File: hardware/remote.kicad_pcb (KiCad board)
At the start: 2 copper layers, 40 x 25 mm, 26 parts, among them P1 CON-SENSOR2, P2 CONN_01X02, U1 XMC1XXX24, U2 RFM69HW, U3 DRILL, U4 DRILL, U5 DRILL, U6 DRILL

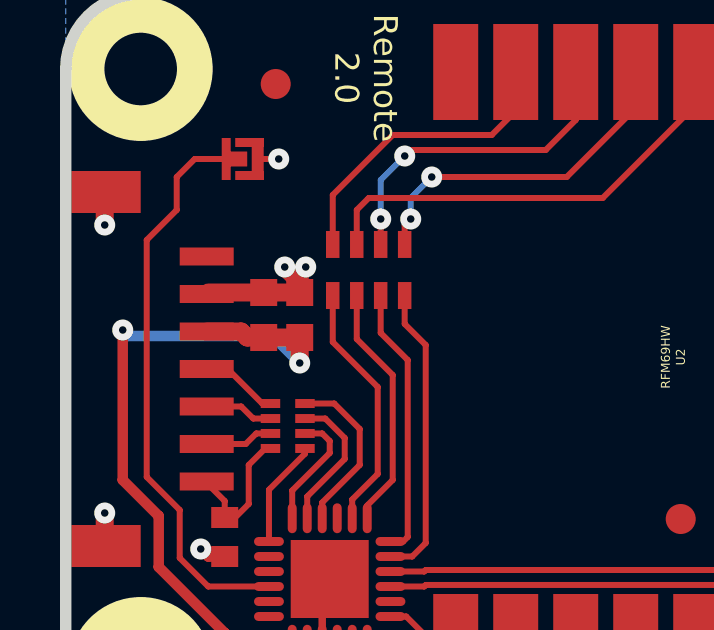
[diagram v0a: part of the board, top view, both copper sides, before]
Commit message: fix capacitor footprints
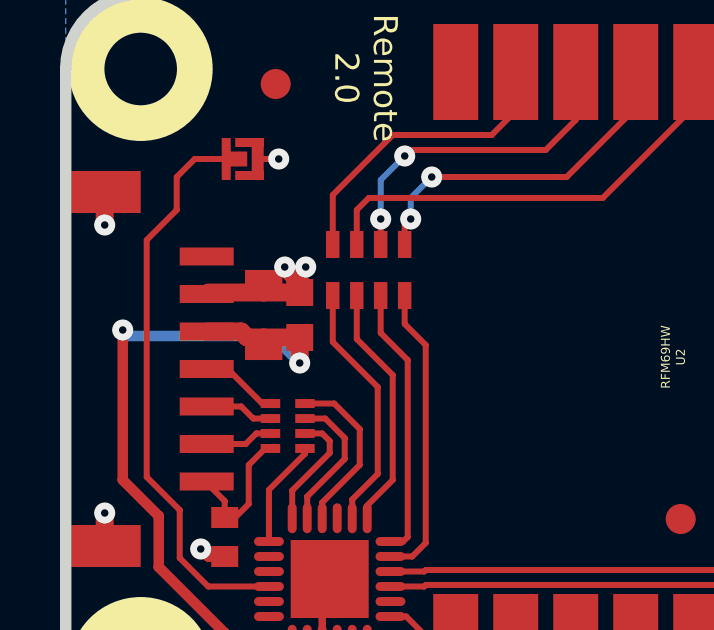
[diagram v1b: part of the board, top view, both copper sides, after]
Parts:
- C2: value 1uF -> 10uF; footprint C0603F -> C0805
- C3: value 10uF -> 1uF
- U2: footprint kicad-libraries:RFM69HW -> RFM69HW
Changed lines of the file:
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@@
   )
   (layers
-    (0 Vorderseite signal hide)
+    (0 Vorderseite signal)
     (31 Rückseite signal hide)
     (32 B.Adhes user)
@@
   )
   (setup
-    (last_trace_width 0.2)
+    (last_trace_width 0.29972)
     (user_trace_width 0.2)
     (user_trace_width 0.25)
@@
   )
   (module C0603F (layer Vorderseite)
-    (at 49.5 40.5 90)
-    (attr smd)
-    (fp_text reference C2 (at 0.05 0.225 90) (layer F.Fab)
-      (effects (font (size 0.2 0.2) (thickness 0.05)))
-    )
-    (fp_text value 1uF (at 0.05 -0.375 90) (layer F.Fab)
-      (effects (font (size 0.2 0.2) (thickness 0.05)))
-    )
-    (fp_line (start -1.45034 -0.65024) (end 1.45034 -0.65024) (layer F.Fab) (width 0.001))
-    (fp_line (start 1.45034 -0.65024) (end 1.45034 0.65024) (layer F.Fab) (width 0.001))
-    (fp_line (start 1.45034 0.65024) (end -1.45034 0.65024) (layer F.Fab) (width 0.001))
-    (fp_line (start -1.45034 0.65024) (end -1.45034 -0.65024) (layer F.Fab) (width 0.001))
-    (pad 1 smd rect (at -0.75 0 90) (size 0.9 0.9) (layers Vorderseite F.Paste F.Mask)
-      (net 2 VCC))
-    (pad 2 smd rect (at 0.75 0 90) (size 0.9 0.9) (layers Vorderseite F.Paste F.Mask)
-      (net 1 GND))
-    (model Capacitors_SMD/C_0603.wrl
-      (at (xyz 0 0 0))
-      (scale (xyz 1 1 1))
-      (rotate (xyz 0 0 0))
-    )
-  )
-  (module C0603F (layer Vorderseite)
     (at 50.7 40.5 90)
     (attr smd)
@@
       (effects (font (size 0.2 0.2) (thickness 0.05)))
     )
-    (fp_text value 10uF (at 0.05 -0.375 90) (layer F.Fab)
+    (fp_text value 1uF (at 0.05 -0.375 90) (layer F.Fab)
       (effects (font (size 0.2 0.2) (thickness 0.05)))
     )
@@
     )
   )
-  (module kicad-libraries:RFM69HW (layer Vorderseite)
-    (at 62.9 41.9 90)
-    (fp_text reference U2 (at 0 0.5 90) (layer F.SilkS)
-      (effects (font (size 0.3 0.3) (thickness 0.075)))
-    )
-    (fp_text value RFM69HW (at 0 0 90) (layer F.SilkS)
-      (effects (font (size 0.3 0.3) (thickness 0.075)))
-    )
-    (fp_line (start -4.85 0.7) (end -4.85 5.85) (layer F.Fab) (width 0.01))
-    (fp_line (start -4.85 5.85) (end 0.4 5.85) (layer F.Fab) (width 0.01))
-    (fp_line (start 0.4 5.85) (end 0.4 0.75) (layer F.Fab) (width 0.01))
-    (fp_line (start 0.4 0.75) (end -4.85 0.75) (layer F.Fab) (width 0.01))
-    (fp_line (start -9.85 -8) (end 9.85 -8) (layer F.Fab) (width 0.01))
-    (fp_line (start 9.85 -8) (end 9.85 8) (layer F.Fab) (width 0.01))
-    (fp_line (start 9.85 8) (end -9.85 8) (layer F.Fab) (width 0.01))
-    (fp_line (start -9.85 8) (end -9.85 -8) (layer F.Fab) (width 0.01))
-    (pad 9 smd rect (at -9.5 -7 90) (size 3.2 1.5) (layers Vorderseite F.Paste F.Mask)
-      (net 23 RESET))
-    (pad 10 smd rect (at -9.5 -5 90) (size 3.2 1.5) (layers Vorderseite F.Paste F.Mask))
-    (pad 11 smd rect (at -9.5 -3 90) (size 3.2 1.5) (layers Vorderseite F.Paste F.Mask)
-      (net 21 DIO1))
-    (pad 12 smd rect (at -9.5 -1 90) (size 3.2 1.5) (layers Vorderseite F.Paste F.Mask)
-      (net 22 DIO2))
-    (pad 13 smd rect (at -9.5 1 90) (size 3.2 1.5) (layers Vorderseite F.Paste F.Mask))
-    (pad 14 smd rect (at -9.5 3 90) (size 3.2 1.5) (layers Vorderseite F.Paste F.Mask))
-    (pad 15 smd rect (at -9.5 5 90) (size 3.2 1.5) (layers Vorderseite F.Paste F.Mask))
-    (pad 16 smd rect (at -9.5 7 90) (size 3.2 1.5) (layers Vorderseite F.Paste F.Mask)
-      (net 2 VCC))
-    (pad 8 smd rect (at 9.5 7 270) (size 3.2 1.5) (layers Vorderseite F.Paste F.Mask)
-      (net 1 GND))
-    (pad 7 smd rect (at 9.5 5 270) (size 3.2 1.5) (layers Vorderseite F.Paste F.Mask)
-      (net 27 Antenna))
-    (pad 6 smd rect (at 9.5 3 270) (size 3.2 1.5) (layers Vorderseite F.Paste F.Mask)
-      (net 1 GND))
-    (pad 5 smd rect (at 9.5 1 270) (size 3.2 1.5) (layers Vorderseite F.Paste F.Mask)
-      (net 14 "Net-(RP2-Pad2)"))
-    (pad 4 smd rect (at 9.5 -1 270) (size 3.2 1.5) (layers Vorderseite F.Paste F.Mask)
-      (net 16 "Net-(RP2-Pad4)"))
-    (pad 3 smd rect (at 9.5 -3 270) (size 3.2 1.5) (layers Vorderseite F.Paste F.Mask)
-      (net 15 "Net-(RP2-Pad3)"))
-    (pad 2 smd rect (at 9.5 -5 270) (size 3.2 1.5) (layers Vorderseite F.Paste F.Mask)
-      (net 13 "Net-(RP2-Pad1)"))
-    (pad 1 smd rect (at 9.5 -7 270) (size 3.2 1.5) (layers Vorderseite F.Paste F.Mask))
-  )
   (module kicad-libraries:WEEE_7mm (layer Rückseite)
     (at 68.9 42.3 180)
@@
       (xy 1.301301 2.715081) (xy 1.302426 2.714986)) (layer B.SilkS) (width 0.01))
   )
+  (module C0805 (layer Vorderseite)
+    (at 49.5 40.5 90)
+    (attr smd)
+    (fp_text reference C2 (at 0 0.3 90) (layer F.Fab)
+      (effects (font (size 0.2 0.2) (thickness 0.05)))
+    )
+    (fp_text value 10uF (at 0 -0.2 90) (layer F.Fab)
+      (effects (font (size 0.2 0.2) (thickness 0.05)))
+    )
+    (fp_line (start -1.651 -0.8001) (end -1.651 0.8001) (layer F.Fab) (width 0.001))
+    (fp_line (start -1.651 0.8001) (end 1.651 0.8001) (layer F.Fab) (width 0.001))
+    (fp_line (start 1.651 0.8001) (end 1.651 -0.8001) (layer F.Fab) (width 0.001))
+    (fp_line (start 1.651 -0.8001) (end -1.651 -0.8001) (layer F.Fab) (width 0.001))
+    (pad 1 smd rect (at -1.00076 0 90) (size 1.00076 1.24968) (layers Vorderseite F.Paste F.Mask)
+      (net 2 VCC) (clearance 0.14986))
+    (pad 2 smd rect (at 1.00076 0 90) (size 1.00076 1.24968) (layers Vorderseite F.Paste F.Mask)
+      (net 1 GND) (clearance 0.14986))
+    (model Capacitors_SMD/C_0805.wrl
+      (at (xyz 0 0 0))
+      (scale (xyz 1 1 1))
+      (rotate (xyz 0 0 0))
+    )
+  )
+  (module RFM69HW (layer Vorderseite)
+    (at 62.9 41.9 90)
+    (fp_text reference U2 (at 0 0.5 90) (layer F.SilkS)
+      (effects (font (size 0.3 0.3) (thickness 0.075)))
+    )
+    (fp_text value RFM69HW (at 0 0 90) (layer F.SilkS)
+      (effects (font (size 0.3 0.3) (thickness 0.075)))
+    )
+    (fp_line (start -4.85 0.7) (end -4.85 5.85) (layer F.Fab) (width 0.01))
+    (fp_line (start -4.85 5.85) (end 0.4 5.85) (layer F.Fab) (width 0.01))
+    (fp_line (start 0.4 5.85) (end 0.4 0.75) (layer F.Fab) (width 0.01))
+    (fp_line (start 0.4 0.75) (end -4.85 0.75) (layer F.Fab) (width 0.01))
+    (fp_line (start -9.85 -8) (end 9.85 -8) (layer F.Fab) (width 0.01))
+    (fp_line (start 9.85 -8) (end 9.85 8) (layer F.Fab) (width 0.01))
+    (fp_line (start 9.85 8) (end -9.85 8) (layer F.Fab) (width 0.01))
+    (fp_line (start -9.85 8) (end -9.85 -8) (layer F.Fab) (width 0.01))
+    (pad 9 smd rect (at -9.5 -7 90) (size 3.2 1.5) (layers Vorderseite F.Paste F.Mask)
+      (net 23 RESET))
+    (pad 10 smd rect (at -9.5 -5 90) (size 3.2 1.5) (layers Vorderseite F.Paste F.Mask))
+    (pad 11 smd rect (at -9.5 -3 90) (size 3.2 1.5) (layers Vorderseite F.Paste F.Mask)
+      (net 21 DIO1))
+    (pad 12 smd rect (at -9.5 -1 90) (size 3.2 1.5) (layers Vorderseite F.Paste F.Mask)
+      (net 22 DIO2))
+    (pad 13 smd rect (at -9.5 1 90) (size 3.2 1.5) (layers Vorderseite F.Paste F.Mask))
+    (pad 14 smd rect (at -9.5 3 90) (size 3.2 1.5) (layers Vorderseite F.Paste F.Mask))
+    (pad 15 smd rect (at -9.5 5 90) (size 3.2 1.5) (layers Vorderseite F.Paste F.Mask))
+    (pad 16 smd rect (at -9.5 7 90) (size 3.2 1.5) (layers Vorderseite F.Paste F.Mask)
+      (net 2 VCC))
+    (pad 8 smd rect (at 9.5 7 270) (size 3.2 1.5) (layers Vorderseite F.Paste F.Mask)
+      (net 1 GND))
+    (pad 7 smd rect (at 9.5 5 270) (size 3.2 1.5) (layers Vorderseite F.Paste F.Mask)
+      (net 27 Antenna))
+    (pad 6 smd rect (at 9.5 3 270) (size 3.2 1.5) (layers Vorderseite F.Paste F.Mask)
+      (net 1 GND))
+    (pad 5 smd rect (at 9.5 1 270) (size 3.2 1.5) (layers Vorderseite F.Paste F.Mask)
+      (net 14 "Net-(RP2-Pad2)"))
+    (pad 4 smd rect (at 9.5 -1 270) (size 3.2 1.5) (layers Vorderseite F.Paste F.Mask)
+      (net 16 "Net-(RP2-Pad4)"))
+    (pad 3 smd rect (at 9.5 -3 270) (size 3.2 1.5) (layers Vorderseite F.Paste F.Mask)
+      (net 15 "Net-(RP2-Pad3)"))
+    (pad 2 smd rect (at 9.5 -5 270) (size 3.2 1.5) (layers Vorderseite F.Paste F.Mask)
+      (net 13 "Net-(RP2-Pad1)"))
+    (pad 1 smd rect (at 9.5 -7 270) (size 3.2 1.5) (layers Vorderseite F.Paste F.Mask))
+  )
   (gr_line (start 82.9 32.3) (end 82.9 39.1) (angle 90) (layer Edge.Cuts) (width 0.381))

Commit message: fix bootpad name
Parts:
- P2: value CONN_01X02 -> BOOT
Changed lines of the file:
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@@
     (links 56)
     (no_connects 0)
-    (area 42.709499 29.609499 83.090501 54.990501)
+    (area 42.54934 29.609499 282.27147 165.489573)
     (thickness 1.6002)
     (drawings 17)
@@
       (effects (font (size 0.3 0.3) (thickness 0.0712)))
     )
-    (fp_text value CONN_01X02 (at 0 -0.35 180) (layer F.Fab)
+    (fp_text value BOOT (at 0 -0.35 180) (layer F.Fab)
       (effects (font (size 0.3 0.3) (thickness 0.0712)))
     )

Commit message: specify processor
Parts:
- U1: value XMC1XXX24 -> XMC1302-32
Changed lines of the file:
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@@
     (44 Edge.Cuts user)
     (48 B.Fab user)
-    (49 F.Fab user hide)
+    (49 F.Fab user)
   )
   (setup
@@
       (effects (font (size 0.3 0.3) (thickness 0.075)))
     )
-    (fp_text value XMC1XXX24 (at 0 0.8) (layer F.Fab)
+    (fp_text value XMC1302-32 (at 0 0.8) (layer F.Fab)
       (effects (font (size 0.3 0.3) (thickness 0.075)))
     )

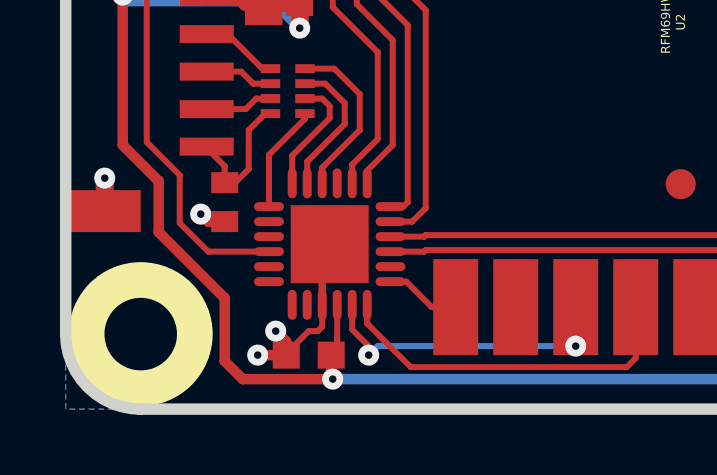
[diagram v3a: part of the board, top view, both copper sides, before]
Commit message: add debug pad
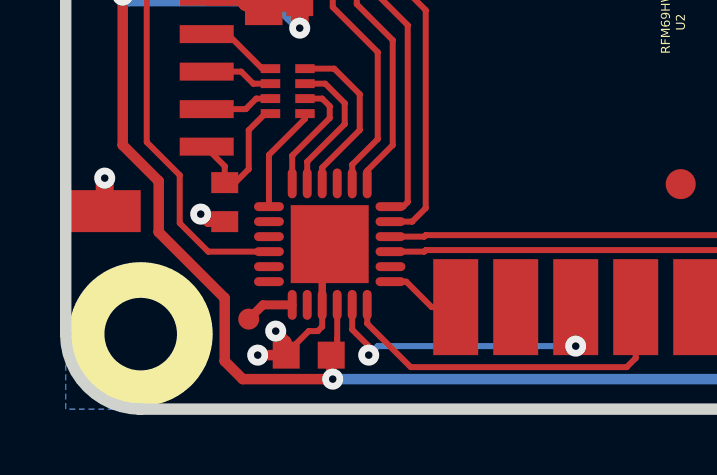
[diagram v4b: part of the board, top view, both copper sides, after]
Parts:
- added J1: Debug, kicad-libraries:DEBUG_PAD, F.Cu at (49.0, 51.8)
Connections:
- U1 pad 7: (no net) -> Net-(J1-Pad1)
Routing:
- net Net-(J1-Pad1): track 0.00 -> 1.65 mm
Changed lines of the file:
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@@
 (kicad_pcb (version 4) (host pcbnew 4.0.7-e2-6376~58~ubuntu17.04.1)
   (general
-    (links 56)
+    (links 57)
     (no_connects 0)
-    (area 42.54934 29.609499 282.27147 165.489573)
+    (area 42.709499 29.609499 83.090501 54.990501)
     (thickness 1.6002)
     (drawings 17)
-    (tracks 283)
+    (tracks 285)
     (zones 0)
-    (modules 26)
-    (nets 28)
+    (modules 27)
+    (nets 29)
   )
   (page A4)
@@
   (net 26 "Net-(RP3-Pad4)")
   (net 27 Antenna)
+  (net 28 "Net-(J1-Pad1)")
   (net_class Default "Dies ist die voreingestellte Netzklasse."
     (clearance 0.15)
@@
     (add_net "Net-(D1-Pad2)")
     (add_net "Net-(D2-Pad2)")
+    (add_net "Net-(J1-Pad1)")
     (add_net "Net-(P1-Pad4)")
     (add_net "Net-(P1-Pad5)")
@@
     (pad 5 smd oval (at -2.025 0.75) (size 1 0.3) (layers Vorderseite F.Paste F.Mask))
     (pad 6 smd oval (at -2.025 1.25) (size 1 0.3) (layers Vorderseite F.Paste F.Mask))
-    (pad 7 smd oval (at -1.25 2.025 90) (size 1 0.3) (layers Vorderseite F.Paste F.Mask))
+    (pad 7 smd oval (at -1.25 2.025 90) (size 1 0.3) (layers Vorderseite F.Paste F.Mask)
+      (net 28 "Net-(J1-Pad1)"))
     (pad 8 smd oval (at -0.75 2.025 90) (size 1 0.3) (layers Vorderseite F.Paste F.Mask))
     (pad 9 smd oval (at -0.25 2.025 90) (size 1 0.3) (layers Vorderseite F.Paste F.Mask)
@@
     (pad 1 smd rect (at 9.5 -7 270) (size 3.2 1.5) (layers Vorderseite F.Paste F.Mask))
   )
+  (module kicad-libraries:DEBUG_PAD (layer Vorderseite)
+    (at 49 51.8)
+    (fp_text reference J1 (at 0 0.175) (layer F.Fab)
+      (effects (font (size 0.15 0.15) (thickness 0.0375)))
+    )
+    (fp_text value Debug (at 0 -0.15) (layer F.Fab)
+      (effects (font (size 0.15 0.15) (thickness 0.0375)))
+    )
+    (pad 1 smd circle (at 0 0) (size 0.7 0.7) (layers Vorderseite F.Paste F.Mask)
+      (net 28 "Net-(J1-Pad1)"))
+  )
   (gr_line (start 82.9 32.3) (end 82.9 39.1) (angle 90) (layer Edge.Cuts) (width 0.381))
   (gr_line (start 82.9 45.1) (end 82.9 52.3) (angle 90) (layer Edge.Cuts) (width 0.381))
@@
   (segment (start 69.8 42.1) (end 72.6 42.1) (width 0.8001) (layer Vorderseite) (net 27))
   (segment (start 67.9 40.2) (end 69.8 42.1) (width 0.8001) (layer Vorderseite) (net 27))
+  (segment (start 50.45 51.325) (end 49.475 51.325) (width 0.29972) (layer Vorderseite) (net 28))
+  (segment (start 49.475 51.325) (end 49 51.8) (width 0.29972) (layer Vorderseite) (net 28))
   (zone (net 1) (net_name GND) (layer Vorderseite) (hatch edge 0.508)
     (connect_pads yes (clearance 0.15))
